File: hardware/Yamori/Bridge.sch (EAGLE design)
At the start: 14 parts, among them J1 CONN_20X2, U3 SN74LS244N

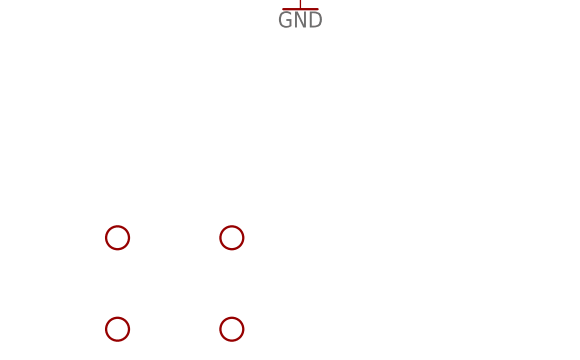
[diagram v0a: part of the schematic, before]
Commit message: Holes removed
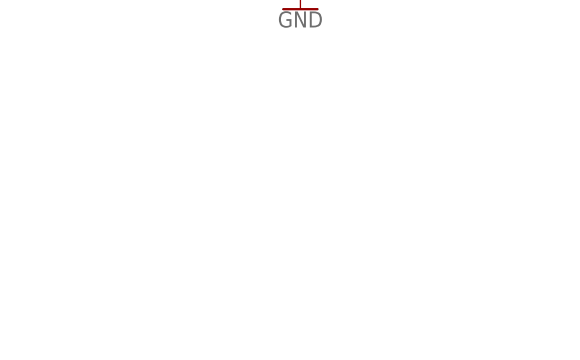
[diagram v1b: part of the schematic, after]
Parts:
- removed H1, H2, H3, H4: STAND-OFF, SparkFun-Hardware:STAND-OFF
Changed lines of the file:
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@@
 <part name="SUPPLY2" library="SparkFun-PowerSymbols" deviceset="5V" device=""/>
 <part name="GND1" library="SparkFun-PowerSymbols" deviceset="GND" device=""/>
-<part name="H1" library="SparkFun-Hardware" deviceset="STAND-OFF" device=""/>
-<part name="H2" library="SparkFun-Hardware" deviceset="STAND-OFF" device=""/>
-<part name="H3" library="SparkFun-Hardware" deviceset="STAND-OFF" device=""/>
-<part name="H4" library="SparkFun-Hardware" deviceset="STAND-OFF" device=""/>
 <part name="S1" library="SparkFun-Switches" deviceset="MOMENTARY-SWITCH-SPST" device="-PTH-6.0MM"/>
 <part name="J3" library="SparkFun-Connectors" deviceset="CONN_10" device="&quot;"/>
@@
 <attribute name="VALUE" x="7.62" y="42.926" size="1.778" layer="96" align="top-center"/>
 </instance>
-<instance part="H1" gate="G$1" x="-73.66" y="-35.56" smashed="yes"/>
-<instance part="H2" gate="G$1" x="-60.96" y="-35.56" smashed="yes"/>
-<instance part="H3" gate="G$1" x="-73.66" y="-45.72" smashed="yes"/>
-<instance part="H4" gate="G$1" x="-60.96" y="-45.72" smashed="yes"/>
 <instance part="S1" gate="G$1" x="12.7" y="-5.08" smashed="yes" rot="R90">
 <attribute name="NAME" x="11.176" y="-5.08" size="1.778" layer="95" font="vector" rot="R90" align="bottom-center"/>

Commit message: Schema final version
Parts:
- R3: value (none) -> 4.7K
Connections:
- net BTN1 renamed !BTN1
- net PWR_OFF renamed !PWR_OFF
- removed net BCM13: J4.5
- net BCM3: now also J4.5

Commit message: Wiring in progress
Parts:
- added H1, H2: STAND-OFF, SparkFun-Hardware:STAND-OFF
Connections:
- net BCM22: now also J4.18
- net BCM24: no longer J4.18
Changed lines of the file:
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@@
 <part name="S2" library="SparkFun-Switches" deviceset="MOMENTARY-SWITCH-SPST" device="-PTH-6.0MM"/>
 <part name="GND6" library="SparkFun-PowerSymbols" deviceset="GND" device=""/>
+<part name="H1" library="SparkFun-Hardware" deviceset="STAND-OFF" device=""/>
+<part name="H2" library="SparkFun-Hardware" deviceset="STAND-OFF" device=""/>
 </parts>
 <sheets>
@@
 <attribute name="VALUE" x="40.64" y="-18.034" size="1.778" layer="96" align="top-center"/>
 </instance>
+<instance part="H1" gate="G$1" x="160.02" y="88.9" smashed="yes"/>
+<instance part="H2" gate="G$1" x="160.02" y="81.28" smashed="yes"/>
 </instances>
 <busses>
@@
 <label x="-81.28" y="63.5" size="1.778" layer="95"/>
 </segment>
+<segment>
+<pinref part="J4" gate="G$1" pin="18"/>
+<wire x1="99.06" y1="0" x2="109.22" y2="0" width="0.1524" layer="91"/>
+<label x="101.6" y="0" size="1.778" layer="95"/>
+</segment>
 </net>
 <net name="BCM23" class="0">
@@
 <label x="73.66" y="5.08" size="1.778" layer="95"/>
 </segment>
-<segment>
-<pinref part="J4" gate="G$1" pin="18"/>
-<wire x1="99.06" y1="0" x2="109.22" y2="0" width="0.1524" layer="91"/>
-<label x="101.6" y="0" size="1.778" layer="95"/>
-</segment>
-</net>
+</net>
